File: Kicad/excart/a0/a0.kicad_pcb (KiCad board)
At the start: 2 copper layers, 7 parts, among them J1 Conn_02x17_Odd_Even, U1 SST39SF040, U2 74LS174, U3 74HC138

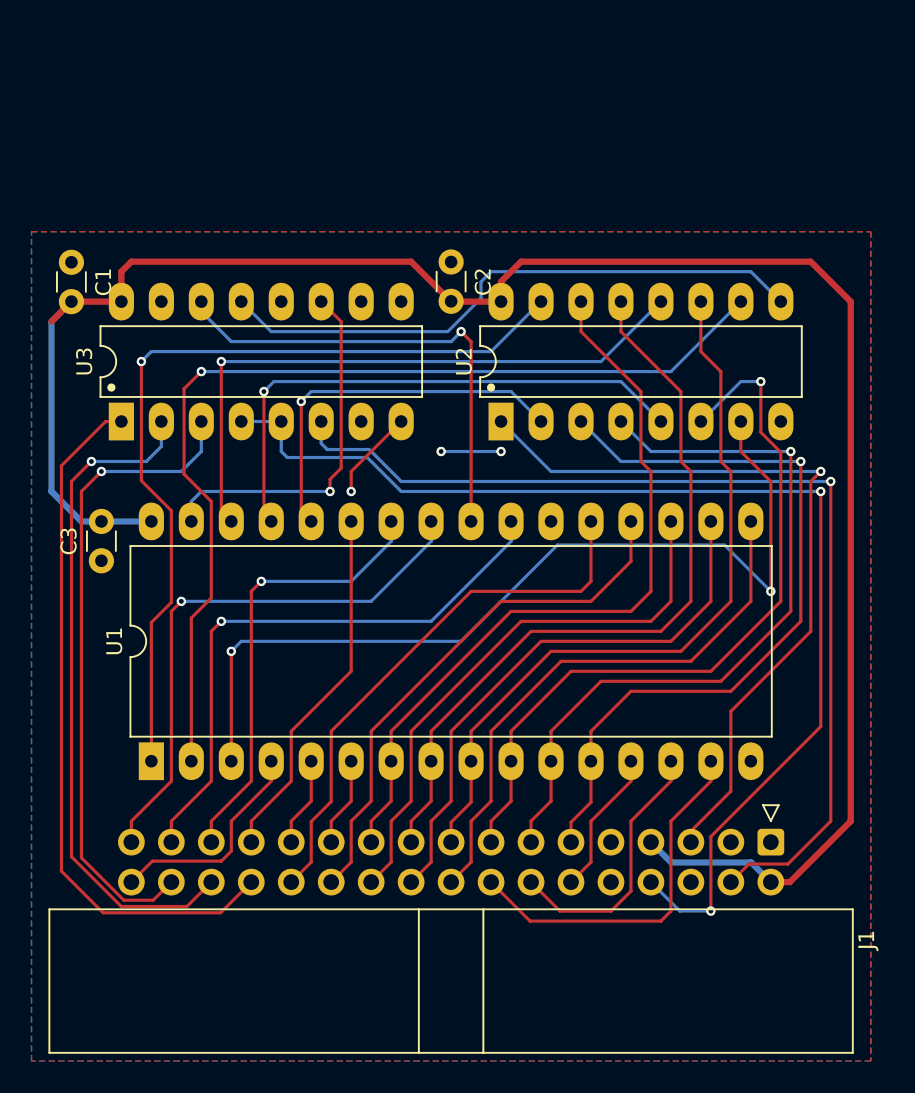
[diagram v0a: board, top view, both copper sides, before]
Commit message: Add TTL/MIC level jumper to trs jack
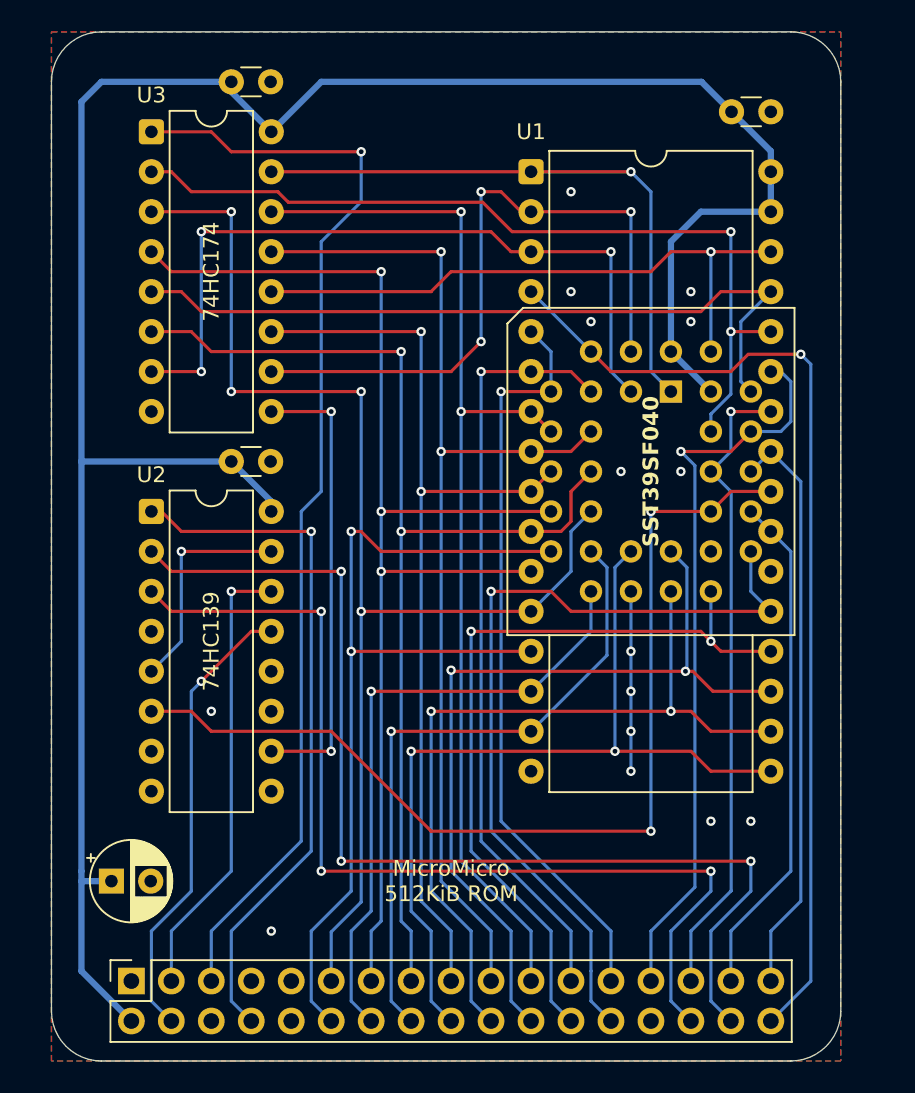
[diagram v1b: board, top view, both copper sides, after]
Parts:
- added C4: C_Polarized, Capacitor_THT:CP_Radial_D5.0mm_P2.50mm, F.Cu at (121.9, 144.8)
- J1: value Conn_02x17_Odd_Even -> IDC 34; footprint Connector_IDC:IDC-Header_2x17_P2.54mm_Horizontal -> Connector_PinSocket_2.54mm:PinSocket_2x17_P2.54mm_Vertical
- U1: footprint Package_DIP:DIP-32_W15.24mm_LongPads -> Global:PLCC-DIP-32_THT-Socket
- U2: value 74LS174 -> 74HC139; footprint PCM_Package_DIP_AKL:DIP-16_W7.62mm_LongPads -> Package_DIP:DIP-16_W7.62mm
- U3: value 74HC138 -> 74HC174; footprint PCM_Package_DIP_AKL:DIP-16_W7.62mm_LongPads -> Package_DIP:DIP-16_W7.62mm
- moved J1 41.6 mm to (123.2, 151.1), turned to 90 degrees
- moved U1 40.5 mm to (157.5, 113.7), turned to 0 degrees
- moved U2 22.9 mm to (124.5, 121.3), turned to 0 degrees
- moved C2 20.2 mm to (161.3, 95.9), turned to 0 degrees
- moved U3 18.5 mm to (124.5, 97.2), turned to 0 degrees
- moved C1 15.3 mm to (129.5, 94.0), turned to 0 degrees
- moved C3 10.4 mm to (129.5, 118.1), turned to 0 degrees
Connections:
- C1 pad 1: GND -> VCC
- C1 pad 2: VCC -> GND
- C2 pad 1: GND -> VCC
- C2 pad 2: VCC -> GND
- C3 pad 1: GND -> VCC
- C3 pad 2: VCC -> GND
- J1 pad 3: /M16 -> /16Mhz
- J1 pad 7: VCC -> /RAMHIDE
- U1 pad 24: /ExROMRd -> Net-(U1-OE)
- U1 pad 31: /ExROMWr -> VCC
- U2 pad 1: /~{RESET} -> /~{A15}
- U2 pad 10: Net-(U1-A16) -> Net-(U2B-O2)
- U2 pad 11: /A3 -> unconnected-(U2B-O1-Pad11)
- U2 pad 12: Net-(U1-A17) -> unconnected-(U2B-O0-Pad12)
- U2 pad 13: /A4 -> /ø2
- U2 pad 14: /A5 -> /16Mhz
- U2 pad 15: Net-(U1-A18) -> Net-(U2A-O1)
- U2 pad 2: Net-(U1-A13) -> /A13
- U2 pad 3: /A0 -> /A14
- U2 pad 4: /A1 -> unconnected-(U2A-O0-Pad4)
- U2 pad 5: Net-(U1-A14) -> Net-(U2A-O1)
- U2 pad 6: /A2 -> Net-(U1-OE)
- U2 pad 7: Net-(U1-A15) -> unconnected-(U2A-O3-Pad7)
- U2 pad 9: /ExReg -> unconnected-(U2B-O3-Pad9)
- U3 pad 1: /A15 -> /~{RESET}
- U3 pad 10: unconnected-(U3-~{Y5}-Pad10) -> Net-(U1-A16)
- U3 pad 11: /ExROMWr -> /A3
- U3 pad 12: unconnected-(U3-~{Y3}-Pad12) -> Net-(U1-A17)
- U3 pad 13: /ExReg -> /A4
- U3 pad 14: /ExROMRd -> /A5
- U3 pad 15: unconnected-(U3-~{Y0}-Pad15) -> Net-(U1-A18)
- U3 pad 2: /A14 -> Net-(U1-A13)
- U3 pad 3: /A13 -> /A0
- U3 pad 4: /~{A15} -> /A1
- U3 pad 5: /~{A15} -> Net-(U1-A14)
- U3 pad 6: /ø2 -> /A2
- U3 pad 7: unconnected-(U3-~{Y7}-Pad7) -> Net-(U1-A15)
- U3 pad 9: unconnected-(U3-~{Y6}-Pad9) -> Net-(U2B-O2)
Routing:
- net Net-(U1-OE): track 0.00 -> 62.7 mm, vias 0 -> 2
- net /A12: track 13.9 -> 63.4 mm, vias 0 -> 1
- net /D0: track 9.26 -> 57.3 mm, vias 0 -> 2
- net /A15: track 44.7 -> 0.00 mm
- net /A6: track 5.67 -> 48.6 mm, vias 0 -> 1
- net /A7: track 5.67 -> 47.9 mm, vias 0 -> 1
- net /ExReg: track 38.1 -> 0.00 mm
- net /ø2: track 64.3 -> 29.2 mm
- net /A1: track 47.7 -> 80.8 mm, vias 1 -> 3
- net /A0: track 49.0 -> 81.7 mm, vias 1 -> 4
- net /ExROMRd: track 30.5 -> 0.00 mm, vias 1 -> 0
- net Net-(U1-A13): track 24.2 -> 54.2 mm, vias 1 -> 2
- net /~{A15}: track 73.9 -> 44.2 mm, vias 2 -> 1
- net Net-(U2B-O2): track 0.00 -> 29.2 mm, vias 0 -> 2
- net /16Mhz: track 0.00 -> 28.9 mm, vias 0 -> 1
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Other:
- board outline added: 50.2 x 65.4 mm
- board text added: "MicroMicro 512KiB ROM"
